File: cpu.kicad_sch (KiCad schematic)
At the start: 55 parts, among them IC11 NM(TO220), IC12 NJM2845DL1-33, J11 Conn_01x03, J12 Conn_01x06_Female, J13 Conn_01x09_Female, J14 Conn_01x07_Socket, J15 Conn_01x07_Socket, J16 Conn_01x06_Female, J17 Conn_01x08_Female, J18 USB_C_POW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

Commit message: Add files via upload
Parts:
- removed J17: Conn_01x08_Female, Connector_PinHeader_2.54mm:PinHeader_1x08_P2.54mm_Vertical, symbol Connector:Conn_01x08_Female
- added J17: Conn_01x06_Female, UserLib:PinHeader_1x06_P2.54mm_Vertical, symbol Connector:Conn_01x06_Female
- C19: value 0.1u -> 1u
- C21: value 1u -> NM
- R25: value NM -> 10k
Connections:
- net +5V: no longer R25.1
- net GND: now also J17.1 (Pin_1)
- net M5_3.3V: no longer C17.1, D13.1 (K), R14.1, R15.1, R20.1, R21.1, R28.1
- net M5_EN: now also J17.3 (Pin_3)
- net M5_IO0: now also J17.2 (Pin_2)
- net M5_P25: now also R25.2
- net M5_RXD: now also J17.4 (Pin_4)
- net M5_TXD: now also J17.5 (Pin_5)
- net at J15.3 (Pin_3), J16.1 (Pin_1), R28.2: now also R25.1, J17.6 (Pin_6)
- new net LMT_3.3V: C17.1, D13.1 (K), R14.1, R15.1, R20.1, R21.1, R28.1
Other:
- note removed: "N.C."
- note removed: "R7 Yaesu 4.7k Standard 22k ICOM 22k KENWOOD open"
- moved on the sheet: S2

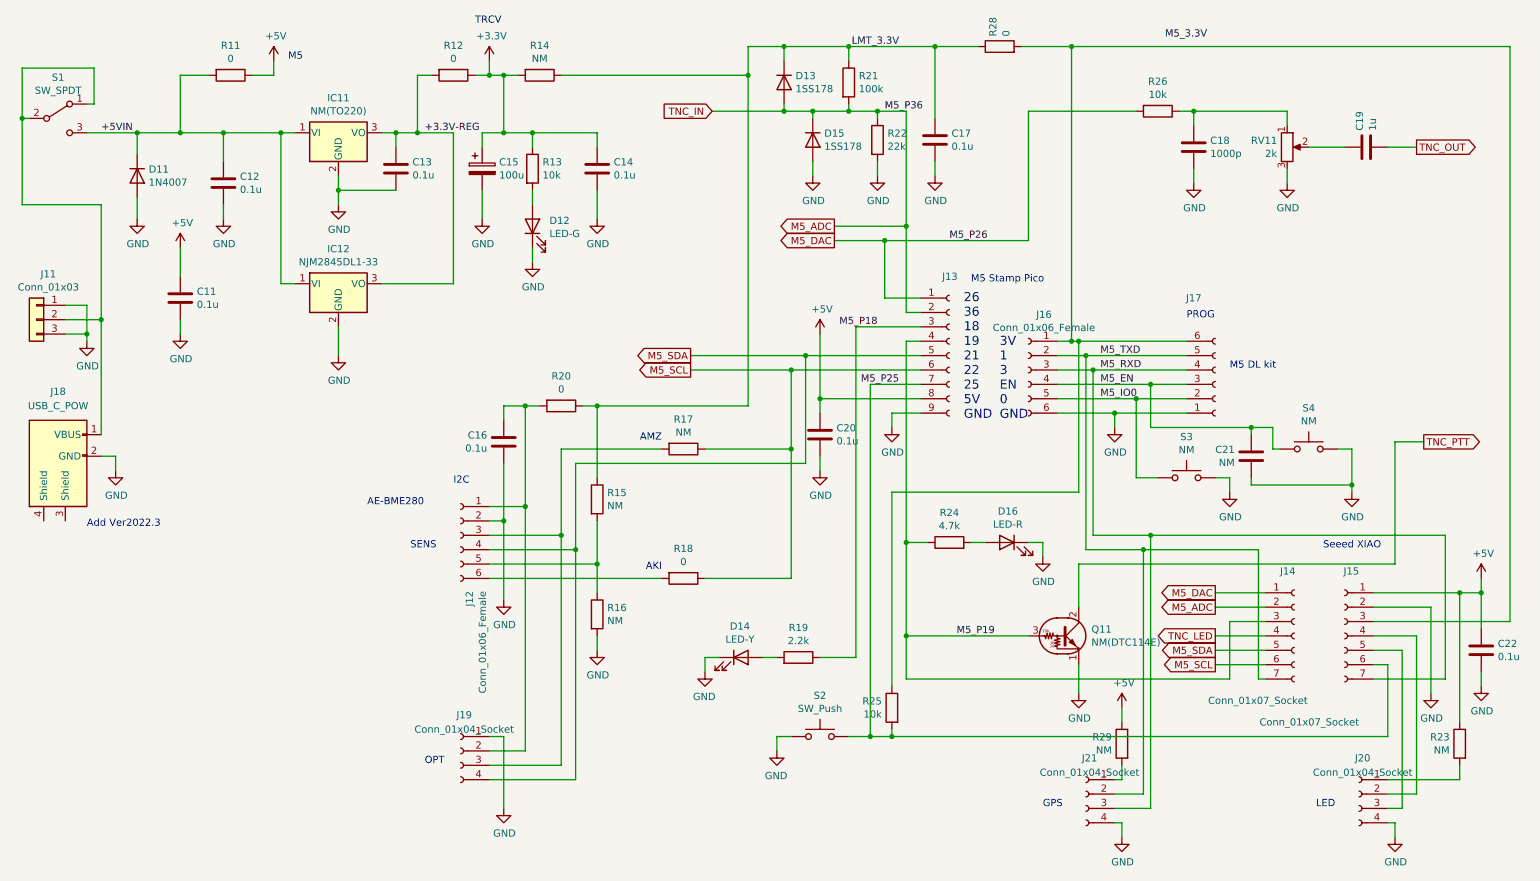
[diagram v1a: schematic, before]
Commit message: CAD data update
CADデータを更新
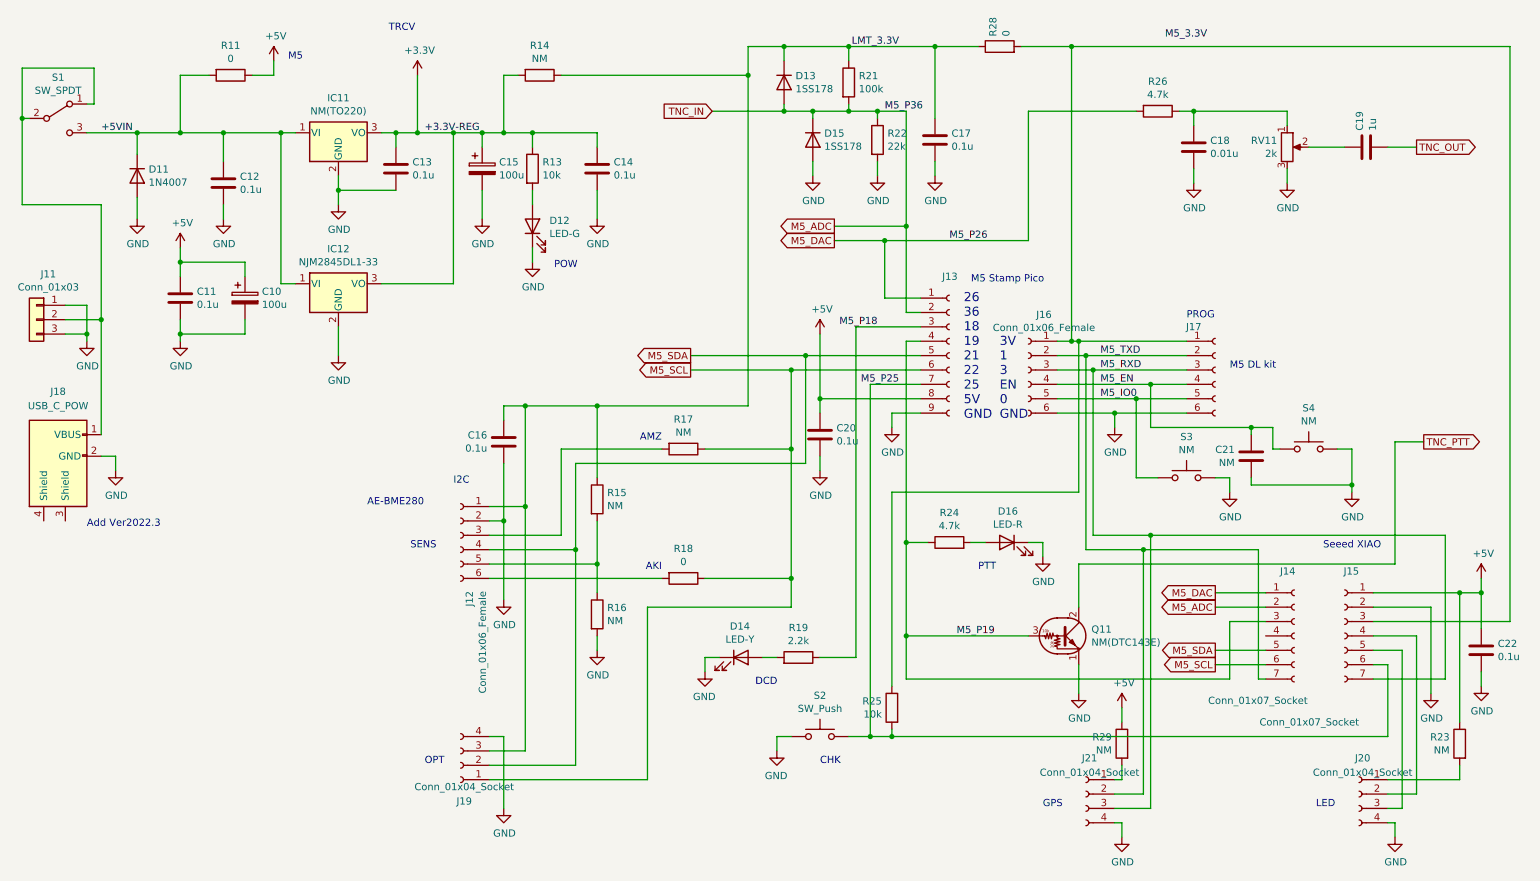
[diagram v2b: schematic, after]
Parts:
- removed R12, R20: 0, Resistor_THT:R_Axial_DIN0207_L6.3mm_D2.5mm_P2.54mm_Vertical, symbol Device:R
- added C10: 100u, Capacitor_THT:CP_Radial_D4.0mm_P2.00mm, symbol Device:CP
- C18: value 1000p -> 0.01u
- Q11: value NM(DTC114E) -> NM(DTC143E)
- R26: value 10k -> 4.7k
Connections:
- net +3.3V-REG is gone; now on net +3V3: C13.1, IC11.3 (VO), IC12.3 (VO)
- net +5V: now also C10.1
- net GND: now also J17.6 (Pin_6), J19.4 (Pin_4), C10.2; no longer J17.1 (Pin_1), J19.1 (Pin_1)
- net LMT_3.3V: now also C16.1, J12.1 (Pin_1), J19.3 (Pin_3)
- net M5_EN: now also J17.4 (Pin_4); no longer J17.3 (Pin_3)
- net M5_IO0: now also J17.5 (Pin_5); no longer J17.2 (Pin_2)
- net M5_RXD: now also J17.3 (Pin_3); no longer J17.4 (Pin_4)
- net M5_SCL: now also J19.1 (Pin_1)
- net M5_SDA: now also J19.2 (Pin_2); no longer J19.4 (Pin_4)
- net M5_TXD: now also J17.2 (Pin_2); no longer J17.5 (Pin_5)
- net at J15.3 (Pin_3), J16.1 (Pin_1), R25.1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: now also J17.1 (Pin_1); no longer J17.6 (Pin_6)
- net at J12.3 (Pin_3), R17.2: no longer J19.3 (Pin_3)
- net TNC_LED: no longer names the net of J14.4 (Pin_4)
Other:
- note added: "CHK"
- note added: "DCD"
- note added: "POW"
- note added: "PTT"
- moved on the sheet: J19
